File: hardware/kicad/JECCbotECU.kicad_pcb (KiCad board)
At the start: 2 copper layers, 100 x 60 mm, 72 parts, among them CN1 ADAFRUIT_FEATHER, P1 USB_B, U2 BSS138, U3 BSS138, U5 TPS54335A, U6 GAPTEC_6S8W4_1.6RP, U7 LT1117, Y1 Crystal_Small

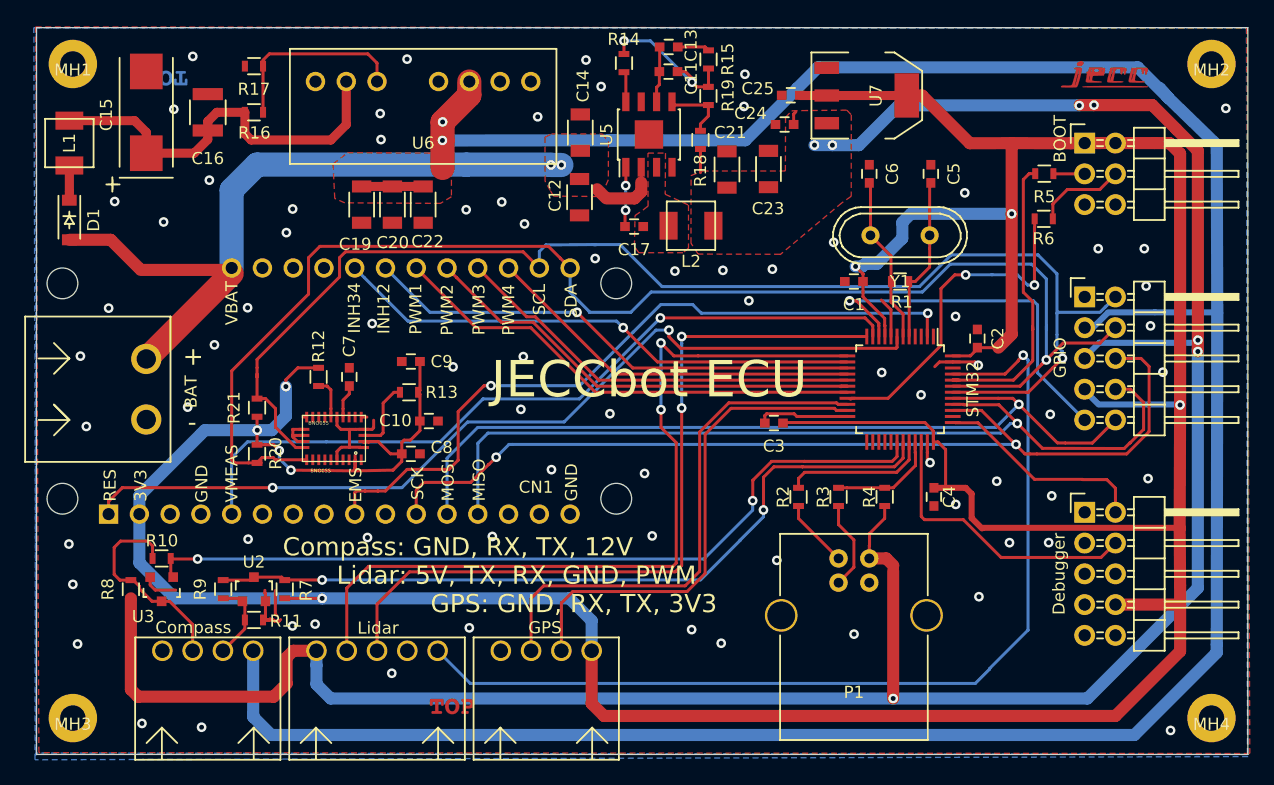
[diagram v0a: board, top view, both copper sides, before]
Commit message: updated schematics
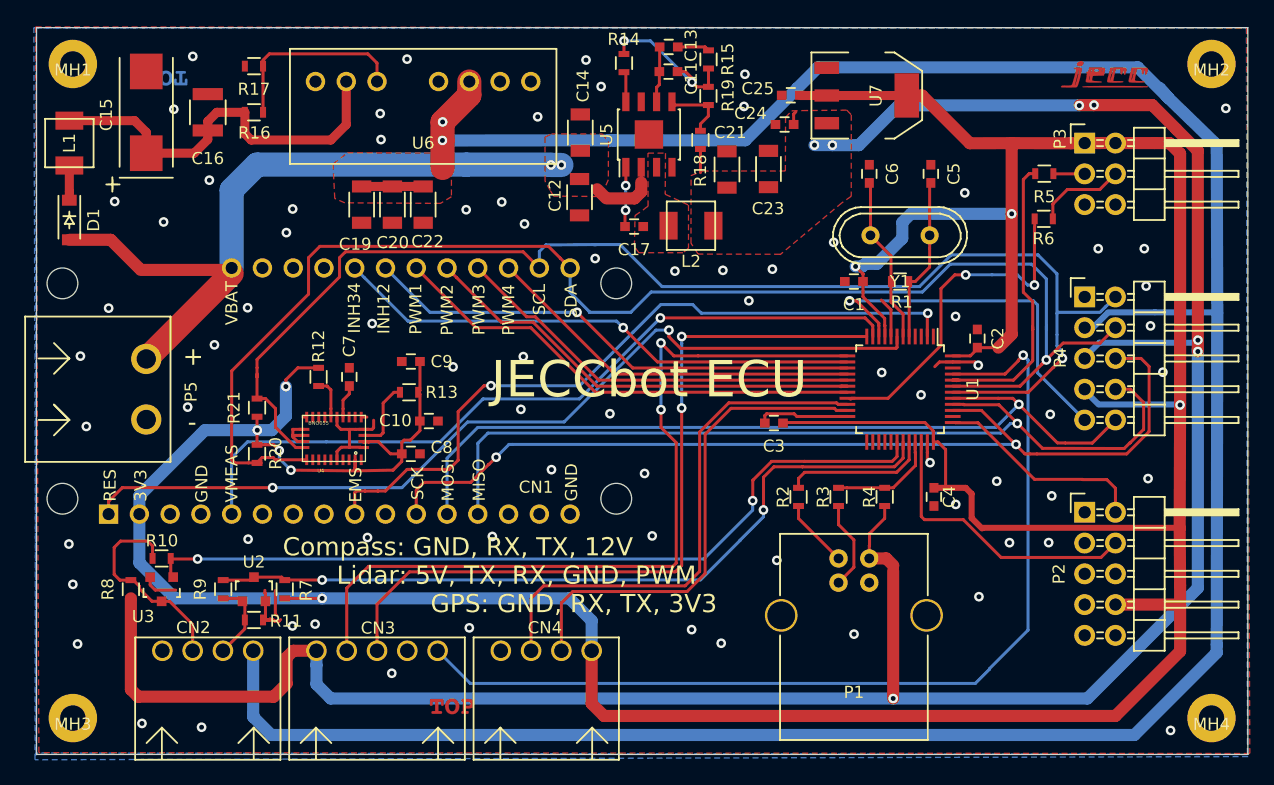
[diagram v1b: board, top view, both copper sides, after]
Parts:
- renumbered Compass to CN2, Lidar to CN3, GPS to CN4, Debugger to P2, BOOT to P3, GPIO to P4, BAT to P5, STM32 to U1, BNO055 to U4
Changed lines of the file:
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@@
   (module mechanical-connectors:WR-TBL_691313710002 (layer F.Cu)
     (at 99.06 69.85 270)
-    (fp_text reference BAT (at 0.21336 -3.69316 90) (layer F.SilkS)
+    (fp_text reference P5 (at 0.21336 -3.69316 90) (layer F.SilkS)
       (effects (font (size 1 1) (thickness 0.15)))
     )
@@
   (module LGA:LGA-28-5832 (layer F.Cu)
     (at 114.554 73.914 180)
-    (fp_text reference BNO055 (at 1.0922 -2.66192) (layer F.SilkS)
+    (fp_text reference U4 (at 1.0922 -2.66192) (layer F.SilkS)
       (effects (font (size 0.3 0.3) (thickness 0.075)))
     )
@@
     (tags "QFP 0.5")
     (attr smd)
-    (fp_text reference STM32 (at 0 -6 90) (layer F.SilkS)
+    (fp_text reference U1 (at 0 -6 90) (layer F.SilkS)
       (effects (font (size 1 1) (thickness 0.15)))
     )
@@
     (descr "Through hole pin header")
     (tags "pin header")
-    (fp_text reference GPIO (at -2.02184 5.01904 90) (layer F.SilkS)
+    (fp_text reference P4 (at -2.02184 5.01904 90) (layer F.SilkS)
       (effects (font (size 1 1) (thickness 0.15)))
     )
@@
     (descr "Through hole pin header")
     (tags "pin header")
-    (fp_text reference BOOT (at -2.032 -0.3556 90) (layer F.SilkS)
+    (fp_text reference P3 (at -2.032 -0.3556 90) (layer F.SilkS)
       (effects (font (size 1 1) (thickness 0.15)))
     )
@@
     (descr "Through hole pin header")
     (tags "pin header")
-    (fp_text reference Debugger (at -2.11836 5.08508 90) (layer F.SilkS)
+    (fp_text reference P2 (at -2.11836 5.08508 90) (layer F.SilkS)
       (effects (font (size 1 1) (thickness 0.15)))
     )
@@
     (at 132.08 91.44)
     (tags "WR-TBL Series 382 2.50 mm Horizontal PCB Header")
-    (fp_text reference GPS (at -0.10668 -1.905) (layer F.SilkS)
+    (fp_text reference CN4 (at -0.10668 -1.905) (layer F.SilkS)
       (effects (font (size 1 1) (thickness 0.15)))
     )
@@
     (at 118.11 91.44)
     (tags "WR-TBL Series 382 2.50 mm Horizontal PCB Header")
-    (fp_text reference Lidar (at 0.08128 -1.87452) (layer F.SilkS)
+    (fp_text reference CN3 (at 0.08128 -1.87452) (layer F.SilkS)
       (effects (font (size 1 1) (thickness 0.15)))
     )
@@
     (at 104.14 91.44)
     (tags "WR-TBL Series 382 2.50 mm Horizontal PCB Header")
-    (fp_text reference Compass (at -1.1938 -1.92024) (layer F.SilkS)
-      (effects (font (size 1 1) (thickness 0.15)))
-    )
+    (fp_text reference CN2 (at -1.1938 -1.92024) (layer F.SilkS)
+      (effects (font (size 1 1) (thickness 0.15)))
+    )

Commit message: moved top label
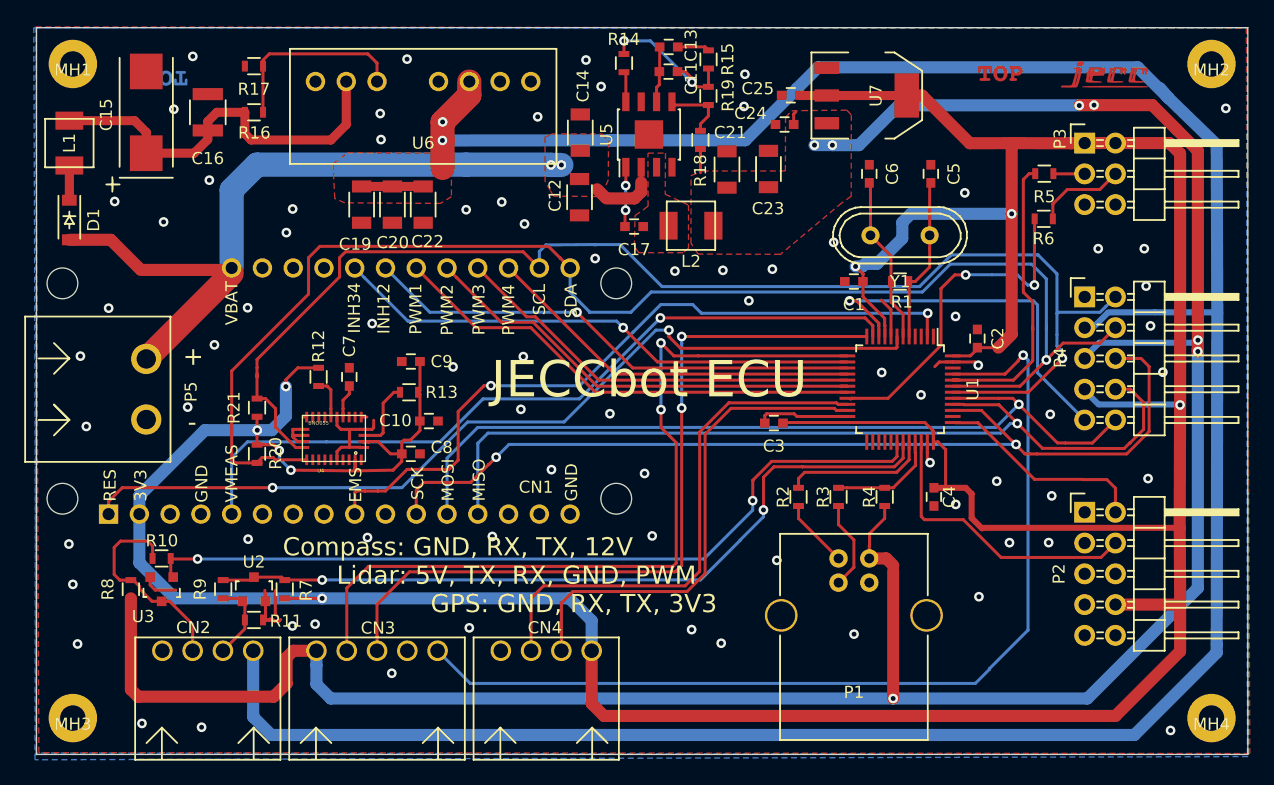
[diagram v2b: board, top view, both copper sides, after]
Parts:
- moved G*** 69.1 mm to (169.6, 43.8)
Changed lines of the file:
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@@
   )
   (module labels:Top (layer F.Cu)
-    (at 124.29236 96.04248)
+    (at 169.55008 43.7896)
     (descr "Top Label")
     (tags "Label Top")

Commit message: renamed
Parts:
- renumbered P5 to BAT, U4 to BNO055, P3 to Boot, CN2 to Compass, P2 to Debugger, P4 to GPIO, CN4 to GPS, CN3 to Lidar, U1 to STM32
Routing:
- net GND: vias 77 -> 79
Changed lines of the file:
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@@
     (thickness 1.6)
     (drawings 29)
-    (tracks 884)
+    (tracks 886)
     (zones 0)
     (modules 72)
@@
   (module mechanical-connectors:WR-TBL_691313710002 (layer F.Cu)
     (at 99.06 69.85 270)
-    (fp_text reference P5 (at 0.21336 -3.69316 90) (layer F.SilkS)
+    (fp_text reference BAT (at 0.21336 -3.69316 90) (layer F.SilkS)
       (effects (font (size 1 1) (thickness 0.15)))
     )
@@
   (module LGA:LGA-28-5832 (layer F.Cu)
     (at 114.554 73.914 180)
-    (fp_text reference U4 (at 1.0922 -2.66192) (layer F.SilkS)
+    (fp_text reference BNO055 (at 1.0922 -2.66192) (layer F.SilkS)
       (effects (font (size 0.3 0.3) (thickness 0.075)))
     )
@@
     (tags "QFP 0.5")
     (attr smd)
-    (fp_text reference U1 (at 0 -6 90) (layer F.SilkS)
+    (fp_text reference STM32 (at 0 -6 90) (layer F.SilkS)
       (effects (font (size 1 1) (thickness 0.15)))
     )
@@
     (descr "Through hole pin header")
     (tags "pin header")
-    (fp_text reference P4 (at -2.02184 5.01904 90) (layer F.SilkS)
+    (fp_text reference GPIO (at -2.02184 5.01904 90) (layer F.SilkS)
       (effects (font (size 1 1) (thickness 0.15)))
     )
@@
     (descr "Through hole pin header")
     (tags "pin header")
-    (fp_text reference P3 (at -2.032 -0.3556 90) (layer F.SilkS)
+    (fp_text reference Boot (at -2.032 -0.3556 90) (layer F.SilkS)
       (effects (font (size 1 1) (thickness 0.15)))
     )
@@
     (descr "Through hole pin header")
     (tags "pin header")
-    (fp_text reference P2 (at -2.11836 5.08508 90) (layer F.SilkS)
+    (fp_text reference Debugger (at -2.11836 5.08508 90) (layer F.SilkS)
       (effects (font (size 1 1) (thickness 0.15)))
     )
@@
     (at 132.08 91.44)
     (tags "WR-TBL Series 382 2.50 mm Horizontal PCB Header")
-    (fp_text reference CN4 (at -0.10668 -1.905) (layer F.SilkS)
+    (fp_text reference GPS (at -0.10668 -1.905) (layer F.SilkS)
       (effects (font (size 1 1) (thickness 0.15)))
     )
@@
     (at 118.11 91.44)
     (tags "WR-TBL Series 382 2.50 mm Horizontal PCB Header")
-    (fp_text reference CN3 (at 0.08128 -1.87452) (layer F.SilkS)
+    (fp_text reference Lidar (at 0.08128 -1.87452) (layer F.SilkS)
       (effects (font (size 1 1) (thickness 0.15)))
     )
@@
     (at 104.14 91.44)
     (tags "WR-TBL Series 382 2.50 mm Horizontal PCB Header")
-    (fp_text reference CN2 (at -1.1938 -1.92024) (layer F.SilkS)
+    (fp_text reference Compass (at -1.1938 -1.92024) (layer F.SilkS)
       (effects (font (size 1 1) (thickness 0.15)))
     )
@@
   (segment (start 143.715791 44.102071) (end 143.692931 44.102071) (width 0.25) (layer B.Cu) (net 1))
   (segment (start 144.11579 44.50207) (end 143.715791 44.102071) (width 0.25) (layer B.Cu) (net 1))
-  (via (at 138.49604 41.08958) (size 0.8) (drill 0.4) (layers F.Cu B.Cu) (net 1))
   (segment (start 143.692931 44.102071) (end 140.68044 41.08958) (width 0.25) (layer B.Cu) (net 1))
   (segment (start 140.68044 41.08958) (end 138.49604 41.08958) (width 0.25) (layer B.Cu) (net 1))
@@
   (via (at 148.48332 43.84548) (size 0.8) (drill 0.4) (layers F.Cu B.Cu) (net 1))
   (via (at 148.40712 46.50232) (size 0.8) (drill 0.4) (layers F.Cu B.Cu) (net 1))
-  (via (at 135.36168 42.672) (size 0.8) (drill 0.4) (layers F.Cu B.Cu) (net 1))
-  (via (at 136.61136 44.86148) (size 0.8) (drill 0.4) (layers F.Cu B.Cu) (net 1))
+  (via (at 133.86816 42.70248) (size 0.8) (drill 0.4) (layers F.Cu B.Cu) (net 1))
+  (via (at 135.89 44.77512) (size 0.8) (drill 0.4) (layers F.Cu B.Cu) (net 1))
   (via (at 131.37388 47.36084) (size 0.8) (drill 0.4) (layers F.Cu B.Cu) (net 1))
   (via (at 128.40716 54.39156) (size 0.8) (drill 0.4) (layers F.Cu B.Cu) (net 1))
@@
   (segment (start 165.64 67.6) (end 164.54076 67.6) (width 0.25) (layer F.Cu) (net 1))
   (segment (start 164.54076 67.6) (end 164.15004 67.99072) (width 0.25) (layer F.Cu) (net 1))
+  (via (at 143.47444 47.61484) (size 0.8) (drill 0.4) (layers F.Cu B.Cu) (net 1))
+  (via (at 136.96696 47.23892) (size 0.8) (drill 0.4) (layers F.Cu B.Cu) (net 1))
+  (via (at 168.16832 61.50864) (size 0.8) (drill 0.4) (layers F.Cu B.Cu) (net 1))
   (segment (start 167.088 67.1) (end 165.64 67.1) (width 0.25) (layer F.Cu) (net 2))
   (segment (start 167.628 66.56) (end 167.088 67.1) (width 0.25) (layer F.Cu) (net 2))

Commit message: design rules check
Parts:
- added R22: 220k, resistors:R_0603, F.Cu at (134.0, 44.0)
- added R23: 43.2k, resistors:R_0603, F.Cu at (135.8, 44.0)
- renumbered Debugger to Debug, STM32 to U1, BNO055 to U4
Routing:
- net Net-(R22-Pad2): track 0.00 -> 10.8 mm, vias 0 -> 2
- net VBAT: track 65.3 -> 71.0 mm
- net SPI_MOSI: track 69.4 -> 70.2 mm
- net I2C_SCL: track 108.9 -> 109.7 mm
- net GND: vias 79 -> 77
